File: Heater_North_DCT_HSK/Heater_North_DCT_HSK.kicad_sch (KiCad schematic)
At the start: 3 parts, among them J1 North_Heater_1, J2 North_Heater_2, J3 Internal_Heater_DCT_HSK_Box

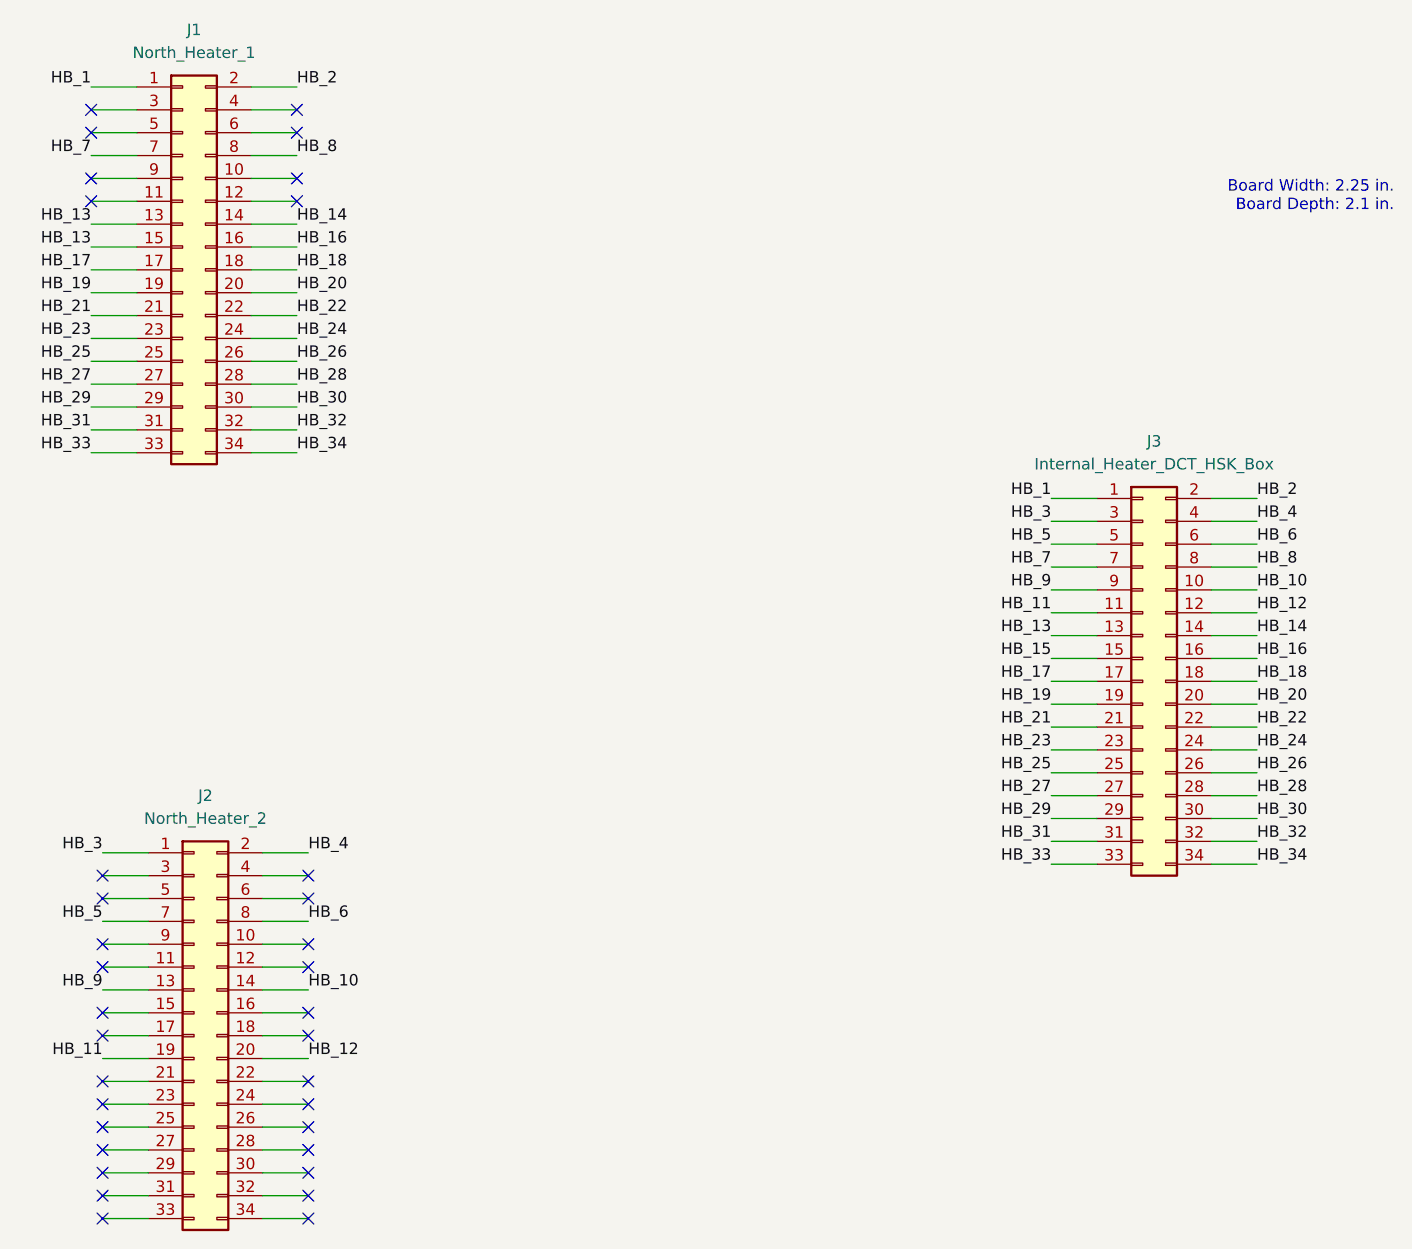
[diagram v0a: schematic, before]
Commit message: Heater norths updated with large track width and mapping, as well as clear labels in schematic. Fits on same width PCB as original, depth is slightly increase and doesn't matter for front panel or box.
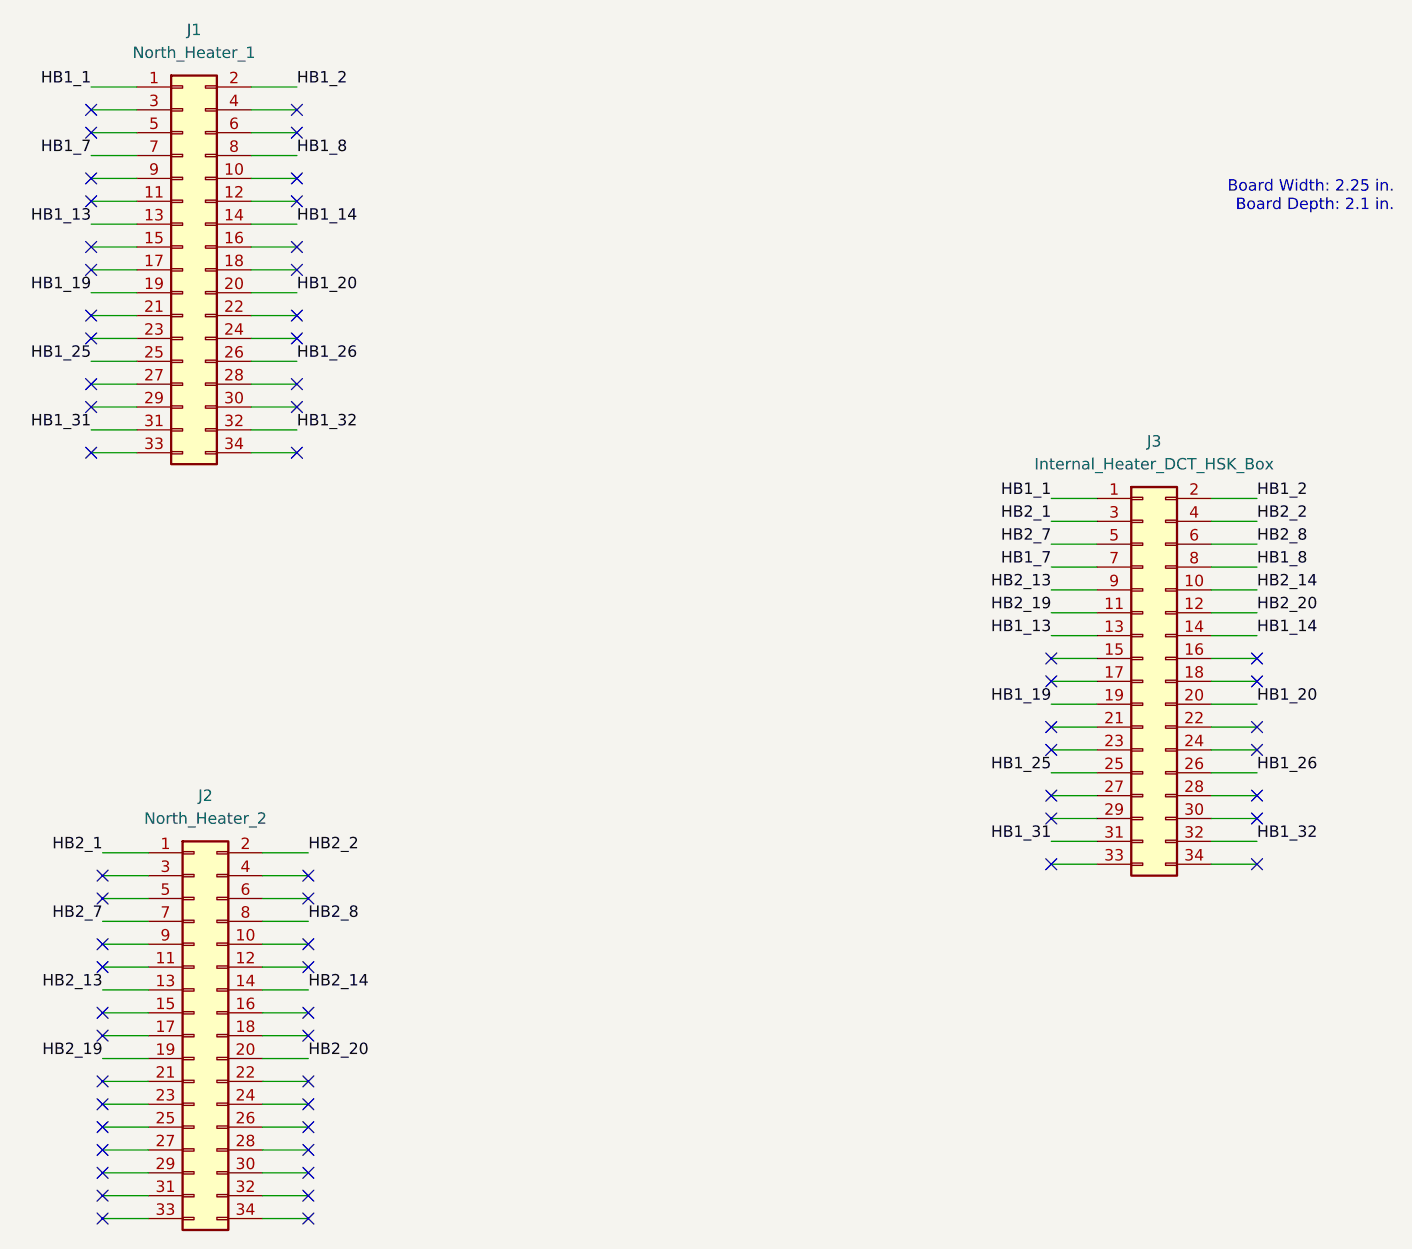
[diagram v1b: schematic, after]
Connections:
- net HB_1 renamed HB1_1
- net HB_10 renamed HB2_14
- net HB_11 renamed HB2_19
- net HB_12 renamed HB2_20
- net HB_13 renamed HB1_13
- net HB1_13: no longer J1.15 (Pin_15)
- net HB_14 renamed HB1_14
- net HB_15: no longer names the net of J3.15 (Pin_15)
- net HB_16: no longer names the net of J3.16 (Pin_16)
- net HB_16: no longer J1.16 (Pin_16)
- net HB_17: no longer names the net of J3.17 (Pin_17)
- net HB_17: no longer J1.17 (Pin_17)
- net HB_18: no longer names the net of J3.18 (Pin_18)
- net HB_18: no longer J1.18 (Pin_18)
- net HB_19 renamed HB1_19
- net HB_2 renamed HB1_2
- net HB_20 renamed HB1_20
- net HB_21: no longer names the net of J3.21 (Pin_21)
- net HB_21: no longer J1.21 (Pin_21)
- net HB_22: no longer names the net of J3.22 (Pin_22)
- net HB_22: no longer J1.22 (Pin_22)
- net HB_23: no longer names the net of J3.23 (Pin_23)
- net HB_23: no longer J1.23 (Pin_23)
- net HB_24: no longer names the net of J3.24 (Pin_24)
- net HB_24: no longer J1.24 (Pin_24)
- net HB_25 renamed HB1_25
- net HB_26 renamed HB1_26
- net HB_27: no longer names the net of J3.27 (Pin_27)
- net HB_27: no longer J1.27 (Pin_27)
- net HB_28: no longer names the net of J3.28 (Pin_28)
- net HB_28: no longer J1.28 (Pin_28)
- net HB_29: no longer names the net of J3.29 (Pin_29)
- net HB_29: no longer J1.29 (Pin_29)
- net HB_3 renamed HB2_1
- net HB_30: no longer names the net of J3.30 (Pin_30)
- net HB_30: no longer J1.30 (Pin_30)
- net HB_31 renamed HB1_31
- net HB_32 renamed HB1_32
- net HB_33: no longer names the net of J3.33 (Pin_33)
- net HB_33: no longer J1.33 (Pin_33)
- net HB_34: no longer names the net of J3.34 (Pin_34)
- net HB_34: no longer J1.34 (Pin_34)
- net HB_4 renamed HB2_2
- net HB_5 renamed HB2_7
- net HB_6 renamed HB2_8
- net HB_7 renamed HB1_7
- net HB_8 renamed HB1_8
- net HB_9 renamed HB2_13
- no-connect marks 34 -> 62
